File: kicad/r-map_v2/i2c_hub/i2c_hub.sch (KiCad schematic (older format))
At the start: 70 parts, among them J1 RJ45, J2 RJ45, J3 RJ45, J4 RJ45, J5 RJ45, P1 5V, P10 CONN_01X04, P11 5V, P12 SEL, P13 3V3, P14 CONN_01X04, P15 5V, P16 SEL, P17 3V3, P18 CONN_01X04, P19 5V, P2 SEL, P20 SEL, P21 3V3, P23 CONN_01X04, P24 5V, P25 SEL, P27 3V3, P28 5V, P29 SEL, P3 3V3, P30 3V3, P31 5V, P32 SEL, P33 3V3, P34 5V, P35 SEL, P36 3V3, P37 5V, P38 SEL, P39 3V3, P4 CONN_01X04, P42 5V, P43 SEL, P44 3V3, P45 CONN_01X04, P46 5V, P47 SEL, P48 3V3, P49 CONN_01X04, P50 5V, P51 SEL, P52 3V3, P53 CONN_01X04, P55 5V, P56 SEL, P57 3V3, P59 CONN_01X04, P6 5V, P60 5V, P61 SEL, P62 3V3, P63 CONN_01X04, P7 SEL, P8 3V3, U1 LM317_SOT223, U2 LM317_SOT223, U3 ESDA6V1-5SC6, U4 ESDA6V1-5SC6, U5 ESDA6V1-5SC6, U6 ESDA6V1-5SC6

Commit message: Add files from last commit on sourceforge
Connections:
- net SCL: now reaches J1.3, J1.4, J2.3, J2.4, J3.3, J3.4, J4.3, J4.4, J5.3, J5.4, P10.2 (P2), P14.2 (P2), P18.2 (P2), P23.2 (P2), P4.2 (P2), P45.2 (P2), P49.2 (P2), P53.2 (P2), P59.2 (P2), P63.2 (P2), U3.5 (IO4), U4.5 (IO4), U5.5 (IO4), U6.5 (IO4)
- net SDA: now reaches J1.5, J1.6, J2.5, J2.6, J3.5, J3.6, J4.5, J4.6, P10.3 (P3), P14.3 (P3), P18.3 (P3), P23.3 (P3), P4.3 (P3), P45.3 (P3), P49.3 (P3), P53.3 (P3), P59.3 (P3), P63.3 (P3), U3.4 (IO3), U4.4 (IO3), U5.4 (IO3), U6.4 (IO3)
- net SDA: now also J5.5, J5.6
- net +5V: now reaches C1.1, P1.1 (P1), P11.1 (P1), P15.1 (P1), P19.1 (P1), P24.1 (P1), P28.1 (P1), P31.1 (P1), P34.1 (P1), P37.1 (P1), P42.1 (P1), P46.1 (P1), P50.1 (P1), P55.1 (P1), P6.1 (P1), P60.1 (P1), U1.3 (IN)
- net +5V: now also C3.1, U2.3 (IN); no longer C4.1, U2.2 (OUT)
- net +3.3V: now reaches C2.1, P13.1 (P1), P17.1 (P1), P21.1 (P1), P27.1 (P1), P3.1 (P1), P30.1 (P1), P33.1 (P1), P36.1 (P1), P39.1 (P1), P44.1 (P1), P48.1 (P1), P52.1 (P1), P57.1 (P1), P62.1 (P1), P8.1 (P1), U1.2 (OUT)
- net +3.3V: now also C4.1, U2.2 (OUT); no longer C3.1, U2.3 (IN)
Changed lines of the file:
@@
 encoding utf-8
 Sheet 1 1
-Title ""
-Date ""
+Title "R-map project - I2C Hub board"
+Date "2015-07-17"
 Rev ""
-Comp ""
-Comment1 ""
+Comp "rmap.cc"
+Comment1 "Author: Daniele Castellari dcast78@gmail.com"
 Comment2 ""
 Comment3 ""
@@
 Wire Wire Line
 	9450 3950 9450 4300
-Wire Wire Line
-	10350 3950 10350 3450
 Connection ~ 9450 3950
-Wire Wire Line
-	8200 3400 8200 3950
 Connection ~ 8400 3950
 Connection ~ 9450 5100
@@
 Wire Wire Line
 	600  3100 600  3450
-Connection ~ 10350 3450
 Wire Wire Line
 	10600 3450 10600 3100
@@
 	8400 3100 8400 3450
 Connection ~ 8400 3450
-Connection ~ 8200 3400
 Wire Wire Line
 	7600 3150 7600 3400
@@
 Wire Wire Line
 	8900 4450 8900 5200
+Text Label 6250 2400 0    60   ~ 0
+GND
+Text Label 6050 2500 0    60   ~ 0
+SDA
+Text Label 5950 2600 0    60   ~ 0
+SCL
+Text Label 5100 3450 2    60   ~ 0
++5V
+Text Label 5100 3400 0    60   ~ 0
++3.3V
+Wire Wire Line
+	7900 2300 7900 2500
+Connection ~ 7900 2500
+Wire Wire Line
+	8200 3450 8200 3950
+Connection ~ 8200 3450
+Wire Wire Line
+	10350 3950 10350 3400
+Connection ~ 10350 3400
 $EndSCHEMATC

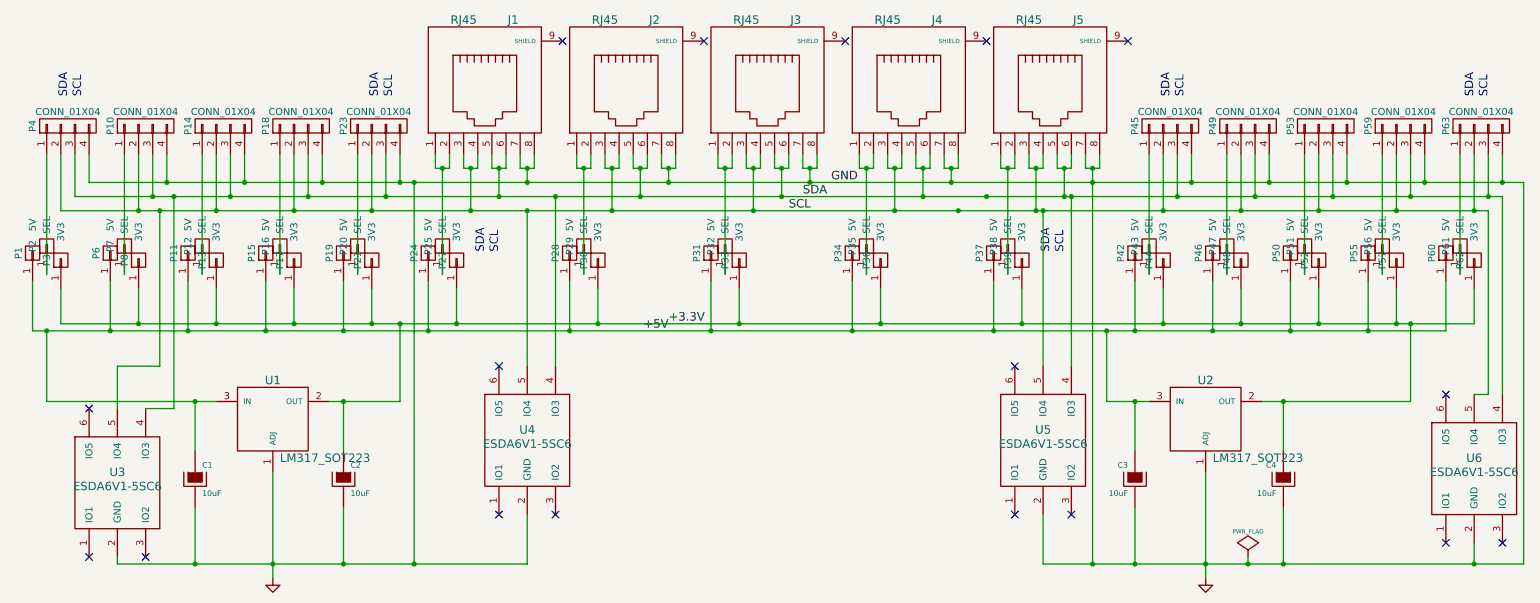
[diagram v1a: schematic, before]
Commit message: Correzioni su board i2c hub, adattamento per uso cavi RJ11, inserite piste per connessioni GND anche in caso taglio board, ricreazione PCB, inserimento riferimenti autore e licenza.
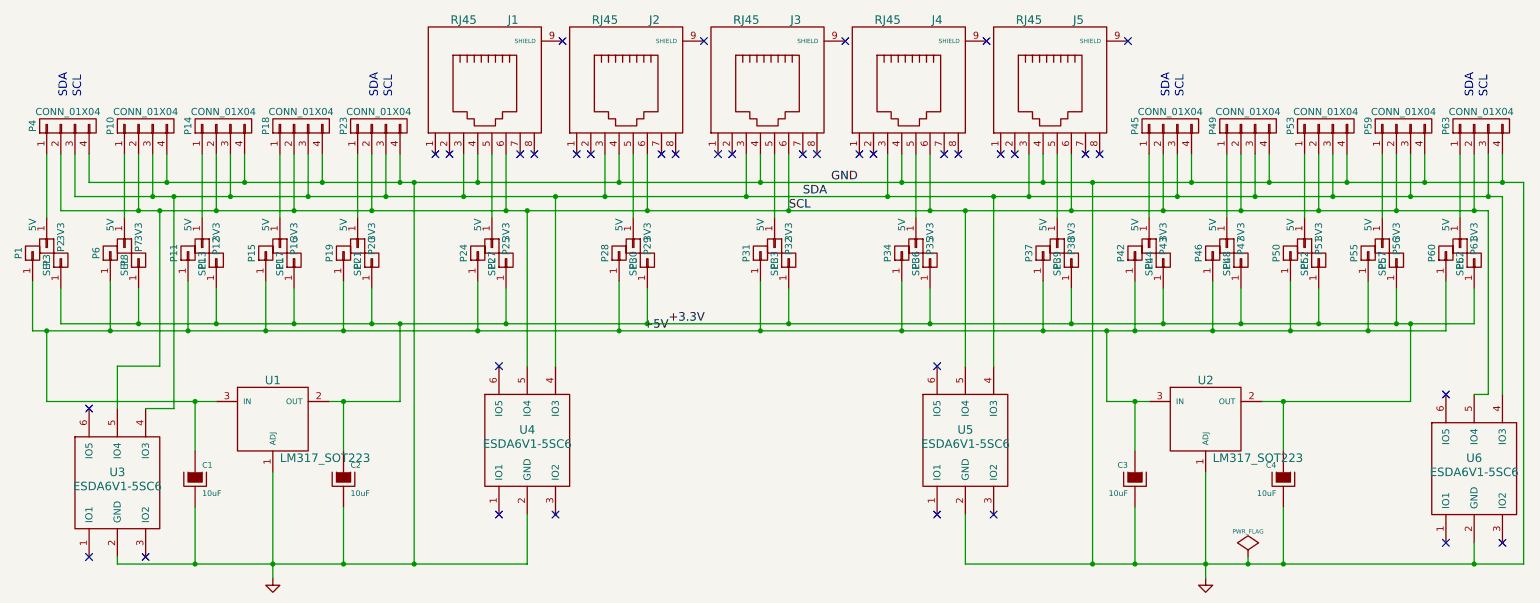
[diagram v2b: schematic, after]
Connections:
- net GND: now also J1.4, J2.4, J3.4, J4.4, J5.4; no longer J1.7, J1.8, J2.7, J2.8, J3.7, J3.8, J4.7, J4.8, J5.7, J5.8
- net SCL: now also J1.6, J2.6, J3.6, J4.6, J5.6; no longer J1.3, J1.4, J2.3, J2.4, J3.3, J3.4, J4.3, J4.4, J5.3, J5.4
- net SDA: now also J1.3, J2.3, J3.3, J4.3, J5.3; no longer J1.5, J1.6, J2.5, J2.6, J3.5, J3.6, J4.5, J4.6, J5.5, J5.6
- new net: J1.5, P25.1 (P1)
- new net: J2.5, P29.1 (P1)
- new net: J3.5, P32.1 (P1)
- new net: J4.5, P35.1 (P1)
- new net: J5.5, P38.1 (P1)
- now unconnected: J1.1, J1.2, J2.1, J2.2, J3.1, J3.2, J4.1, J4.2, J5.1, J5.2
- no-connect marks 17 -> 37
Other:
- moved on the sheet: P12, P16, P2, P20, P24, P25, P27, P28, P29, P30, P31, P32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

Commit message: Aggiunto ponticello a saldare per uscita 3.3V. Nuovo design per i2chub
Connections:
- net +3.3V: now also U3.1 (IO1), U5.1 (IO1), U6.1 (IO1)
- net +5V: now also U3.6 (IO5), U4.1 (IO1), U4.6 (IO5), U5.6 (IO5), U6.6 (IO5)
- no-connect marks 37 -> 29
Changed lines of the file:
@@
 $EndComp
 NoConn ~ 1400 5050
-NoConn ~ 1000 5050
-NoConn ~ 1000 4000
 $Comp
 L ESDA6V1-5SC6 U4
@@
 	1    0    0    -1
 $EndComp
-NoConn ~ 3900 3700
-NoConn ~ 3900 4750
 NoConn ~ 4300 4750
 $Comp
@@
 	1    0    0    -1
 $EndComp
-NoConn ~ 7000 3700
-NoConn ~ 7000 4750
 NoConn ~ 7400 4750
 $Comp
@@
 $EndComp
 NoConn ~ 11000 4950
-NoConn ~ 10600 4950
-NoConn ~ 10600 3900
 $Comp
 L LM317_SOT223 U1
@@
 	1000 2400 11150 2400
 Wire Wire Line
-	11150 5100 11150 2400
+	11150 2400 11150 5100
 Wire Wire Line
 	900  2200 900  2500
@@
 	9450 5100 9450 4700
 Wire Wire Line
-	7200 5100 11150 5100
+	11150 5100 7200 5100
 Wire Wire Line
 	8400 5100 8400 4700
 Wire Wire Line
 	8400 3950 8400 4300
-Wire Wire Line
-	9300 3950 10350 3950
 Wire Wire Line
 	9450 3950 9450 4300
@@
 	10800 3400 10800 3150
 Wire Wire Line
-	800  3400 800  3150
+	800  3150 800  5100
 Wire Wire Line
 	600  3100 600  3450
 Wire Wire Line
-	10600 3450 10600 3100
-Wire Wire Line
-	10250 3150 10250 3400
+	10600 3100 10600 3900
+Wire Wire Line
+	10250 3150 10250 4950
 Connection ~ 10250 3400
 Wire Wire Line
@@
 Connection ~ 3950 3400
 Wire Wire Line
-	3750 3100 3750 3450
+	3750 3100 3750 4750
 Connection ~ 3750 3450
 Wire Wire Line
@@
 	1200 3700 1500 3700
 Wire Wire Line
-	1500 2600 1500 3700
+	1500 3700 1500 2600
 Connection ~ 1500 2600
 Wire Wire Line
@@
 	8200 3950 8500 3950
 Wire Wire Line
-	2700 3950 3200 3950
-Wire Wire Line
 	1200 5100 1200 5050
 Wire Wire Line
@@
 	7950 2200 7950 2600
 Connection ~ 7950 2600
+Connection ~ 10600 3450
+Wire Wire Line
+	10250 4950 10600 4950
+Wire Wire Line
+	1000 4000 1000 3450
+Connection ~ 1000 3450
+Wire Wire Line
+	7000 3700 7000 3450
+Connection ~ 7000 3450
+Wire Wire Line
+	7000 4750 6650 4750
+Wire Wire Line
+	6650 4750 6650 3400
+Connection ~ 6650 3400
+Wire Wire Line
+	3900 3700 3900 3450
+Connection ~ 3900 3450
+Wire Wire Line
+	3750 4750 3900 4750
+Wire Wire Line
+	800  5100 1000 5100
+Connection ~ 800  3400
+Wire Wire Line
+	1000 5100 1000 5050
+Wire Wire Line
+	9300 3950 10350 3950
+Wire Wire Line
+	3200 3950 2700 3950
 $EndSCHEMATC

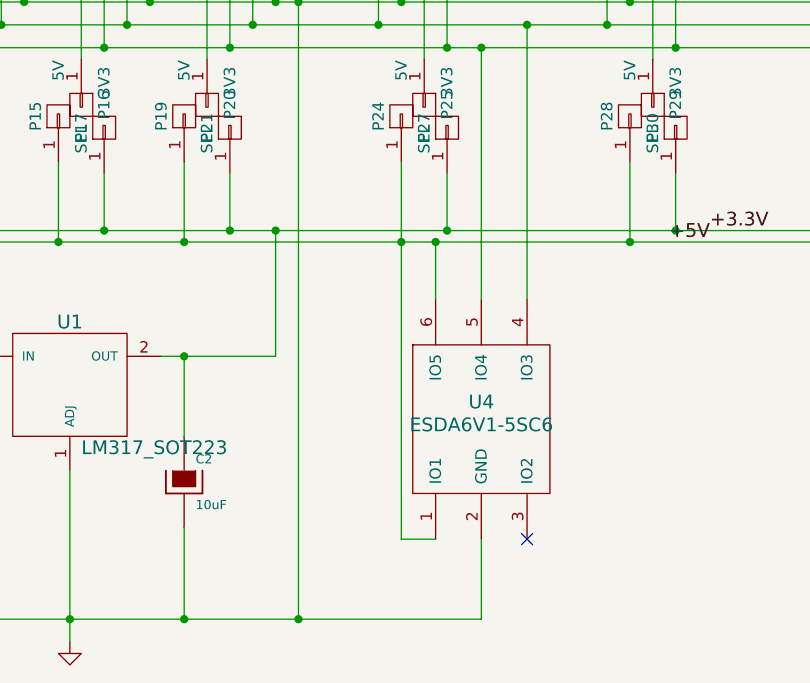
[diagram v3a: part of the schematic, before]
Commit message: modifiche di adeguamento case su stima-th e sistemazione gerber per produzione hub i2c
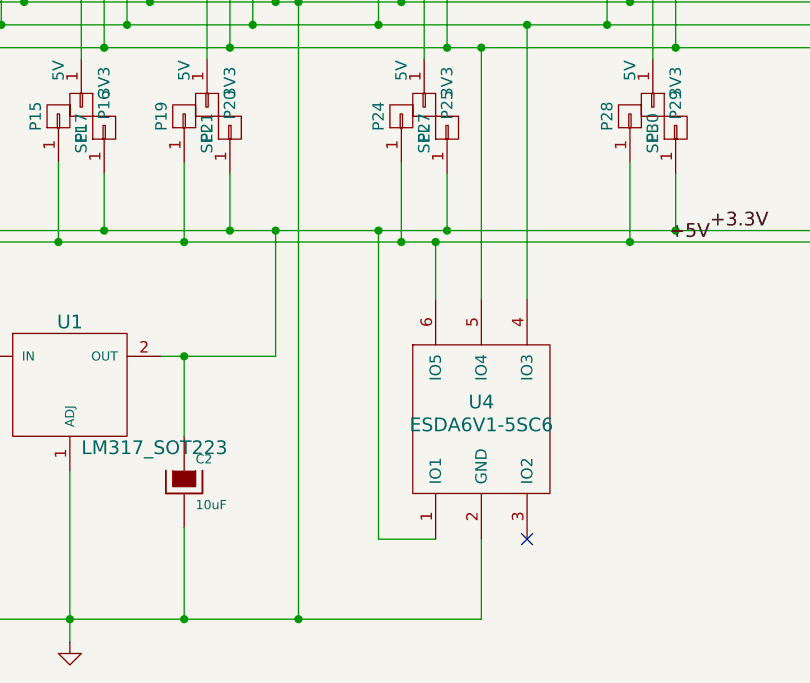
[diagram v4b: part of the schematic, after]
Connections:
- net +3.3V: now also U4.1 (IO1)
- net +5V: no longer U4.1 (IO1)
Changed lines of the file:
@@
 	3950 3150 3950 3400
 Connection ~ 3950 3400
-Wire Wire Line
-	3750 3100 3750 4750
 Connection ~ 3750 3450
 Wire Wire Line
@@
 Connection ~ 3900 3450
 Wire Wire Line
-	3750 4750 3900 4750
+	3650 4750 3900 4750
 Wire Wire Line
 	800  5100 1000 5100
@@
 Wire Wire Line
 	3200 3950 2700 3950
+Wire Wire Line
+	3750 3100 3750 3450
+Wire Wire Line
+	3650 4750 3650 3400
+Connection ~ 3650 3400
 $EndSCHEMATC
